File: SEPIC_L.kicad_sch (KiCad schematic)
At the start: 25 parts, among them IC1 LM5155DSSR, Q1 CSD18537NQ5A

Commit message: REV2
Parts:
- renumbered D3 to D1, R9 to R21, R10 to R22, R11 to R23, R12 to R24, R13 to R25, R14 to R26, R15 to R27, R16 to R28, R17 to R29
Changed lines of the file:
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@@
   (symbol (lib_id "power:GND1") (at 90.805 128.905 0) (unit 1)
     (in_bom yes) (on_board yes) (fields_autoplaced)
-    (property "Reference" "#PWR022" (id 0) (at 90.805 135.255 0)
+    (property "Reference" "#PWR023" (id 0) (at 90.805 135.255 0)
       (effects (font (size 1.27 1.27)) hide)
     )
@@
   (symbol (lib_id "Device:R_US") (at 230.505 81.915 0) (unit 1)
     (in_bom yes) (on_board yes)
-    (property "Reference" "R16" (id 0) (at 233.045 81.915 0))
+    (property "Reference" "R28" (id 0) (at 233.045 81.915 0))
     (property "Value" "51k1" (id 1) (at 234.315 79.375 0))
     (property "Footprint" "Resistor_SMD:R_0603_1608Metric" (id 2) (at 231.521 82.169 90)
@@
   (symbol (lib_id "Device:R_US") (at 230.505 99.695 0) (unit 1)
     (in_bom yes) (on_board yes)
-    (property "Reference" "R17" (id 0) (at 233.045 99.695 0))
+    (property "Reference" "R29" (id 0) (at 233.045 99.695 0))
     (property "Value" "4k7" (id 1) (at 234.315 97.155 0))
     (property "Footprint" "Resistor_SMD:R_0603_1608Metric" (id 2) (at 231.521 99.949 90)
@@
   (symbol (lib_id "power:GND1") (at 131.445 83.185 0) (unit 1)
     (in_bom yes) (on_board yes) (fields_autoplaced)
-    (property "Reference" "#PWR024" (id 0) (at 131.445 89.535 0)
+    (property "Reference" "#PWR025" (id 0) (at 131.445 89.535 0)
       (effects (font (size 1.27 1.27)) hide)
     )
@@
   (symbol (lib_id "power:GND1") (at 167.005 123.825 0) (unit 1)
     (in_bom yes) (on_board yes) (fields_autoplaced)
-    (property "Reference" "#PWR028" (id 0) (at 167.005 130.175 0)
+    (property "Reference" "#PWR029" (id 0) (at 167.005 130.175 0)
       (effects (font (size 1.27 1.27)) hide)
     )
@@
   (symbol (lib_id "power:GND1") (at 67.945 89.535 0) (unit 1)
     (in_bom yes) (on_board yes) (fields_autoplaced)
-    (property "Reference" "#PWR018" (id 0) (at 67.945 95.885 0)
+    (property "Reference" "#PWR019" (id 0) (at 67.945 95.885 0)
       (effects (font (size 1.27 1.27)) hide)
     )
@@
   (symbol (lib_id "power:GND1") (at 230.505 103.505 0) (unit 1)
     (in_bom yes) (on_board yes) (fields_autoplaced)
-    (property "Reference" "#PWR031" (id 0) (at 230.505 109.855 0)
+    (property "Reference" "#PWR032" (id 0) (at 230.505 109.855 0)
       (effects (font (size 1.27 1.27)) hide)
     )
@@
   (symbol (lib_id "Global Symbols:STPS20M100SG-TR") (at 186.055 65.405 0) (unit 1)
     (in_bom yes) (on_board yes) (fields_autoplaced)
-    (property "Reference" "D3" (id 0) (at 192.405 58.3595 0)
+    (property "Reference" "D1" (id 0) (at 192.405 58.3595 0)
       (effects (font (size 1.524 1.524)))
     )
@@
   (symbol (lib_id "power:GND1") (at 90.805 95.885 0) (unit 1)
     (in_bom yes) (on_board yes) (fields_autoplaced)
-    (property "Reference" "#PWR021" (id 0) (at 90.805 102.235 0)
+    (property "Reference" "#PWR022" (id 0) (at 90.805 102.235 0)
       (effects (font (size 1.27 1.27)) hide)
     )
@@
   (symbol (lib_id "Device:R_US") (at 95.885 122.555 0) (unit 1)
     (in_bom yes) (on_board yes) (fields_autoplaced)
-    (property "Reference" "R12" (id 0) (at 97.536 121.6465 0)
+    (property "Reference" "R24" (id 0) (at 97.536 121.6465 0)
       (effects (font (size 1.27 1.27)) (justify left))
     )
@@
   (symbol (lib_id "Device:R_US") (at 80.645 62.865 0) (mirror y) (unit 1)
     (in_bom yes) (on_board yes)
-    (property "Reference" "R10" (id 0) (at 76.835 61.595 0)
+    (property "Reference" "R22" (id 0) (at 76.835 61.595 0)
       (effects (font (size 1.27 1.27)) (justify right))
     )
@@
   (symbol (lib_id "Device:R_US") (at 167.005 118.745 0) (unit 1)
     (in_bom yes) (on_board yes)
-    (property "Reference" "R15" (id 0) (at 169.545 118.745 0))
+    (property "Reference" "R27" (id 0) (at 169.545 118.745 0))
     (property "Value" "4m" (id 1) (at 170.815 116.205 0))
     (property "Footprint" "Resistor_SMD:R_0603_1608Metric" (id 2) (at 168.021 118.999 90)
@@
   (symbol (lib_id "power:GND1") (at 216.535 81.915 0) (unit 1)
     (in_bom yes) (on_board yes) (fields_autoplaced)
-    (property "Reference" "#PWR030" (id 0) (at 216.535 88.265 0)
+    (property "Reference" "#PWR031" (id 0) (at 216.535 88.265 0)
       (effects (font (size 1.27 1.27)) hide)
     )
@@
   (symbol (lib_id "power:GND1") (at 131.445 93.345 0) (unit 1)
     (in_bom yes) (on_board yes) (fields_autoplaced)
-    (property "Reference" "#PWR025" (id 0) (at 131.445 99.695 0)
+    (property "Reference" "#PWR026" (id 0) (at 131.445 99.695 0)
       (effects (font (size 1.27 1.27)) hide)
     )
@@
   (symbol (lib_id "power:GND1") (at 57.785 62.865 0) (unit 1)
     (in_bom yes) (on_board yes) (fields_autoplaced)
-    (property "Reference" "#PWR017" (id 0) (at 57.785 69.215 0)
+    (property "Reference" "#PWR018" (id 0) (at 57.785 69.215 0)
       (effects (font (size 1.27 1.27)) hide)
     )
@@
   (symbol (lib_id "power:GND1") (at 111.125 103.505 0) (unit 1)
     (in_bom yes) (on_board yes) (fields_autoplaced)
-    (property "Reference" "#PWR023" (id 0) (at 111.125 109.855 0)
+    (property "Reference" "#PWR024" (id 0) (at 111.125 109.855 0)
       (effects (font (size 1.27 1.27)) hide)
     )
@@
   (symbol (lib_id "Device:R_US") (at 167.005 111.125 0) (unit 1)
     (in_bom yes) (on_board yes)
-    (property "Reference" "R14" (id 0) (at 169.545 111.125 0))
+    (property "Reference" "R26" (id 0) (at 169.545 111.125 0))
     (property "Value" "4m" (id 1) (at 170.815 108.585 0))
     (property "Footprint" "Resistor_SMD:R_0603_1608Metric" (id 2) (at 168.021 111.379 90)
@@
   (symbol (lib_id "power:GND1") (at 81.915 83.185 0) (unit 1)
     (in_bom yes) (on_board yes) (fields_autoplaced)
-    (property "Reference" "#PWR019" (id 0) (at 81.915 89.535 0)
+    (property "Reference" "#PWR020" (id 0) (at 81.915 89.535 0)
       (effects (font (size 1.27 1.27)) hide)
     )
@@
   (symbol (lib_id "power:GND1") (at 188.595 51.435 0) (unit 1)
     (in_bom yes) (on_board yes) (fields_autoplaced)
-    (property "Reference" "#PWR029" (id 0) (at 188.595 57.785 0)
+    (property "Reference" "#PWR030" (id 0) (at 188.595 57.785 0)
       (effects (font (size 1.27 1.27)) hide)
     )
@@
   (symbol (lib_id "Device:R_US") (at 88.265 83.185 90) (unit 1)
     (in_bom yes) (on_board yes) (fields_autoplaced)
-    (property "Reference" "R11" (id 0) (at 88.265 78.3295 90))
+    (property "Reference" "R23" (id 0) (at 88.265 78.3295 90))
     (property "Value" "17k8" (id 1) (at 88.265 81.1046 90))
     (property "Footprint" "Resistor_SMD:R_0603_1608Metric" (id 2) (at 88.519 82.169 90)
@@
   (symbol (lib_id "Device:R_US") (at 151.765 78.105 270) (unit 1)
     (in_bom yes) (on_board yes)
-    (property "Reference" "R13" (id 0) (at 151.765 83.185 90))
+    (property "Reference" "R25" (id 0) (at 151.765 83.185 90))
     (property "Value" "100" (id 1) (at 151.765 80.645 90))
     (property "Footprint" "Resistor_SMD:R_0603_1608Metric" (id 2) (at 151.511 79.121 90)
@@
   (symbol (lib_id "power:GND1") (at 86.995 65.405 0) (unit 1)
     (in_bom yes) (on_board yes) (fields_autoplaced)
-    (property "Reference" "#PWR020" (id 0) (at 86.995 71.755 0)
+    (property "Reference" "#PWR021" (id 0) (at 86.995 71.755 0)
       (effects (font (size 1.27 1.27)) hide)
     )
@@
   (symbol (lib_id "power:GND1") (at 136.525 66.675 0) (unit 1)
     (in_bom yes) (on_board yes) (fields_autoplaced)
-    (property "Reference" "#PWR026" (id 0) (at 136.525 73.025 0)
+    (property "Reference" "#PWR027" (id 0) (at 136.525 73.025 0)
       (effects (font (size 1.27 1.27)) hide)
     )
@@
   (symbol (lib_id "Device:R_US") (at 70.485 81.915 0) (unit 1)
     (in_bom yes) (on_board yes) (fields_autoplaced)
-    (property "Reference" "R9" (id 0) (at 72.136 81.0065 0)
+    (property "Reference" "R21" (id 0) (at 72.136 81.0065 0)
       (effects (font (size 1.27 1.27)) (justify left))
     )
@@
   (symbol (lib_id "power:GND1") (at 145.415 85.725 0) (unit 1)
     (in_bom yes) (on_board yes) (fields_autoplaced)
-    (property "Reference" "#PWR027" (id 0) (at 145.415 92.075 0)
-      (effects (font (size 1.27 1.27)) hide)
-    )
+    (property "Reference" "#PWR028" (id 0) (at 145.415 92.075 0)
+      (effects (font (size 1.27 1.27)) hide)
+    )

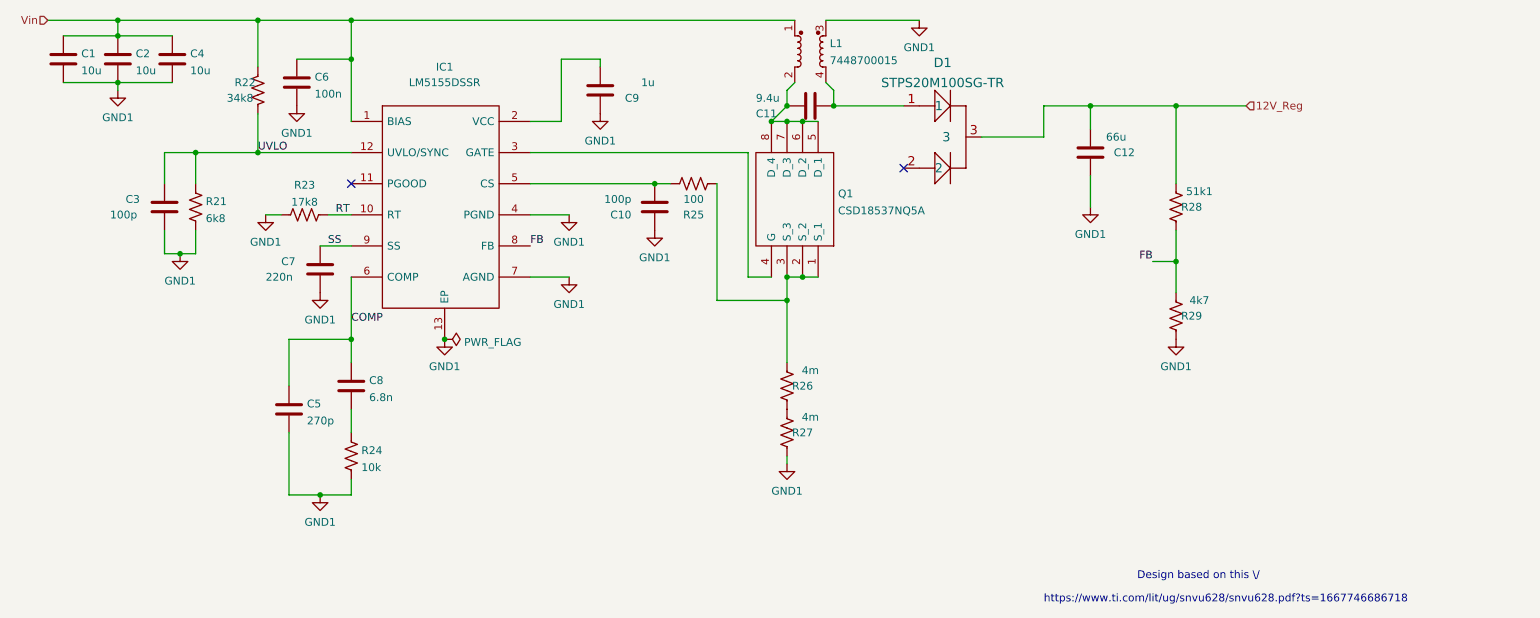
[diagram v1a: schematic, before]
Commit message: changeed caps
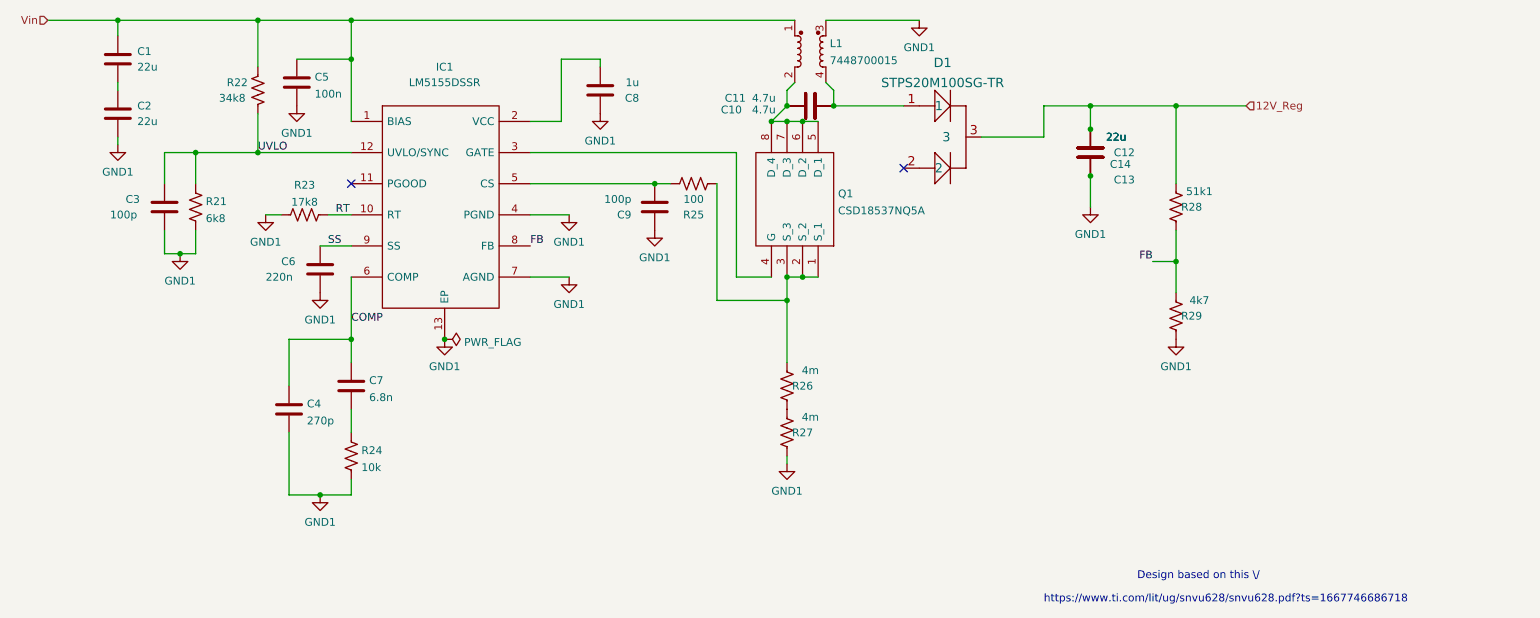
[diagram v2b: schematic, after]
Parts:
- removed C4: 10u, Capacitor_SMD:C_0603_1608Metric, symbol Device:C
- added C11: 4.7u, Capacitor_SMD:C_0805_2012Metric_Pad1.18x1.45mm_HandSolder, symbol Device:C
- added C12, C13: 22u, Capacitor_SMD:C_1206_3216Metric_Pad1.33x1.80mm_HandSolder, symbol Device:C
- C1, C2: value 10u -> 22u; footprint Capacitor_SMD:C_0603_1608Metric -> Capacitor_SMD:C_1206_3216Metric_Pad1.33x1.80mm_HandSolder
- C10: renamed from C11; value 9.4u -> 4.7u; footprint Capacitor_SMD:C_0603_1608Metric -> Capacitor_SMD:C_0805_2012Metric_Pad1.18x1.45mm_HandSolder
- C14: renamed from C12; value 66u -> 22u; footprint Capacitor_SMD:C_0603_1608Metric -> Capacitor_SMD:C_1206_3216Metric_Pad1.33x1.80mm_HandSolder
- C3: footprint Capacitor_SMD:C_0603_1608Metric -> Capacitor_SMD:C_0603_1608Metric_Pad1.08x0.95mm_HandSolder
- C4: renamed from C5; footprint Capacitor_SMD:C_0603_1608Metric -> Capacitor_SMD:C_0603_1608Metric_Pad1.08x0.95mm_HandSolder
- C5: renamed from C6; footprint Capacitor_SMD:C_0603_1608Metric -> Capacitor_SMD:C_0603_1608Metric_Pad1.08x0.95mm_HandSolder
- C6: renamed from C7; footprint Capacitor_SMD:C_0603_1608Metric -> Capacitor_SMD:C_0603_1608Metric_Pad1.08x0.95mm_HandSolder
- C7: renamed from C8; footprint Capacitor_SMD:C_0603_1608Metric -> Capacitor_SMD:C_0603_1608Metric_Pad1.08x0.95mm_HandSolder
- C8: renamed from C9; footprint Capacitor_SMD:C_0603_1608Metric -> Capacitor_SMD:C_0805_2012Metric_Pad1.18x1.45mm_HandSolder
- C9: renamed from C10; footprint Capacitor_SMD:C_0603_1608Metric -> Capacitor_SMD:C_0603_1608Metric_Pad1.08x0.95mm_HandSolder
- R21, R22, R23, R24, R25, R26, R27, R28, R29: footprint Resistor_SMD:R_0603_1608Metric -> Resistor_SMD:R_0603_1608Metric_Pad0.98x0.95mm_HandSolder
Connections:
- net 12V_Reg: now also C12.1, C13.1
- net GND1: now also C12.2, C13.2; no longer C1.2
- net Vin: no longer C2.1
- net at C10.2, L1.2, Q1.5 (D_1)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: now also C11.2
- net at C10.1, D1.1, L1.4: now also C11.1
- new net: C1.2, C2.1
